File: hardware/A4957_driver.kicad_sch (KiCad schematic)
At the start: 21 parts, among them Q1 PSMN1R0-30YLC,115, Q2 PSMN1R0-30YLC,115, Q3 PSMN1R0-30YLC,115, Q4 PSMN1R0-30YLC,115

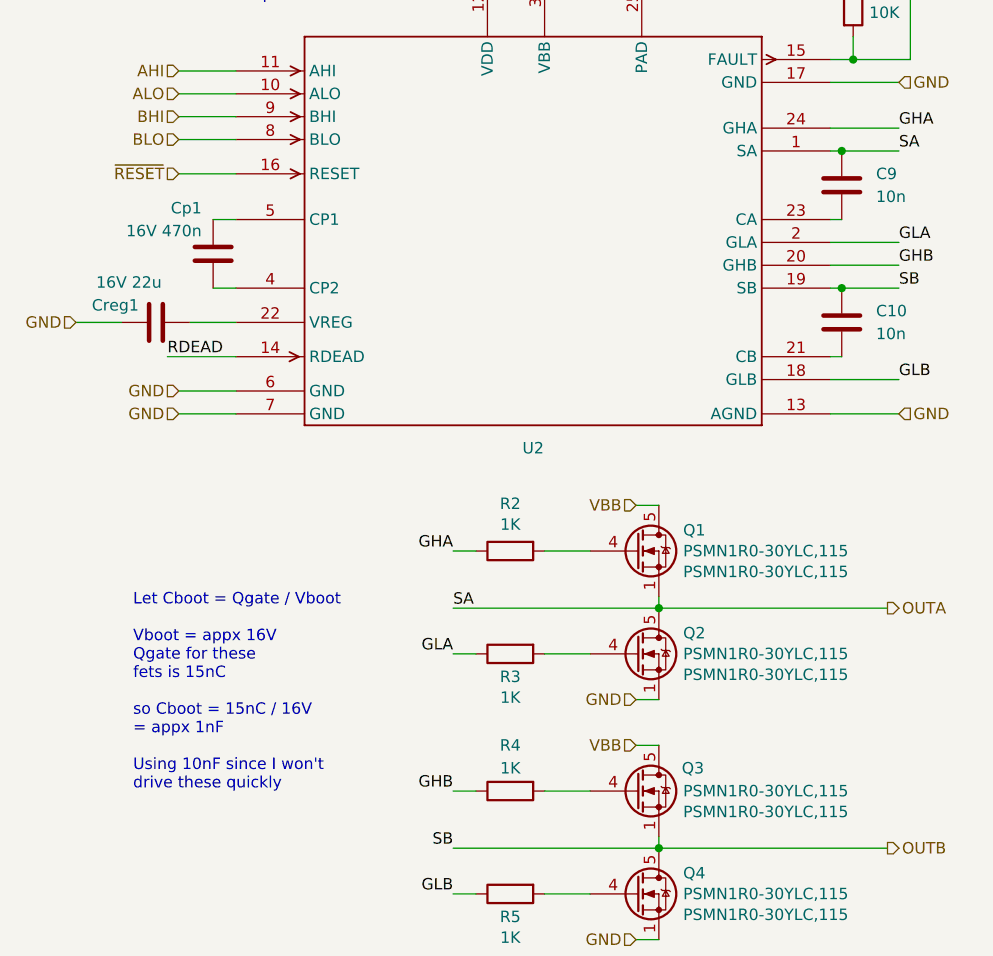
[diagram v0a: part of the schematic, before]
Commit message: initial layout poisitions done
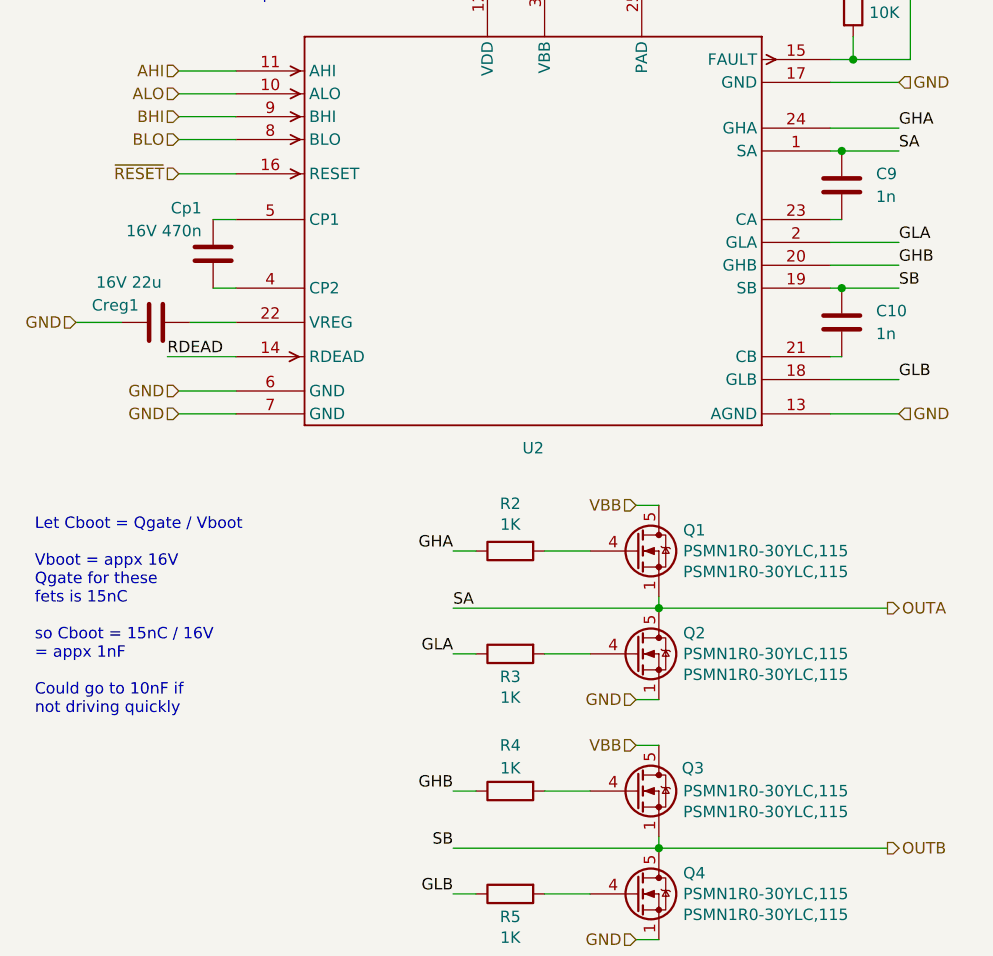
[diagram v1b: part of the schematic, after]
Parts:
- C10, C9: value 10n -> 1n
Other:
- note added: "Let Cboot = Qgate / Vboot Vboot = appx 16V Qgate for these fets is 15nC so Cboot = 15nC / 16V = appx 1nF Could go to 10nF if not driving quickly"
- note removed: "Let Cboot = Qgate / Vboot Vboot = appx 16V Qgate for these fets is 15nC so Cboot = 15nC / 16V = appx 1nF Using 10nF since I won't drive these quickly"
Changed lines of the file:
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@@
 		)
 	)
-	(text "Let Cboot = Qgate / Vboot\n\nVboot = appx 16V\nQgate for these \nfets is 15nC\n\nso Cboot = 15nC / 16V \n= appx 1nF\n\nUsing 10nF since I won't \ndrive these quickly"
-		(exclude_from_sim no)
-		(at 44.45 160.02 0)
+	(text "Let Cboot = Qgate / Vboot\n\nVboot = appx 16V\nQgate for these \nfets is 15nC\n\nso Cboot = 15nC / 16V \n= appx 1nF\n\nCould go to 10nF if\nnot driving quickly"
+		(exclude_from_sim no)
+		(at 33.528 151.638 0)
 		(effects
 			(font
@@
 		(fields_autoplaced yes)
 		(property "Reference" "C10"
-			(at 127 106.68 0)
-			(effects
-				(font
-					(size 1.27 1.27)
-				)
-				(justify left)
-			)
-		)
-		(property "Value" "10n"
-			(at 127 109.22 0)
+			(at 127 106.6799 0)
+			(effects
+				(font
+					(size 1.27 1.27)
+				)
+				(justify left)
+			)
+		)
+		(property "Value" "1n"
+			(at 127 109.2199 0)
 			(effects
 				(font
@@
 		(fields_autoplaced yes)
 		(property "Reference" "C9"
-			(at 127 91.44 0)
-			(effects
-				(font
-					(size 1.27 1.27)
-				)
-				(justify left)
-			)
-		)
-		(property "Value" "10n"
-			(at 127 93.98 0)
-			(effects
-				(font
+			(at 127 91.4399 0)
+			(effects
+				(font
+					(size 1.27 1.27)
+				)
+				(justify left)
+			)
+		)
+		(property "Value" "1n"
+			(at 127 93.9799 0)
+			(effects
+				(font

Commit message: set repo
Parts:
- C10, C9: value 1n -> 1nF; footprint Capacitor_SMD:C_0603_1608Metric -> Capacitor_SMD:C_0805_2012Metric
- C11: value 50V 10U -> 50V 10uF
- C5: value 10U -> 10uF
- C6: value 100N -> 100nF; footprint Capacitor_SMD:C_0603_1608Metric -> Capacitor_SMD:C_0805_2012Metric
- C7, C8: value 50V 220U -> 50V 220uF
- Cp1: value 16V 470n -> 16V 470nF
- Creg1: value 16V 22u -> 16V 22uF
- JP1, R1, R2, R3, R4, R5, R6: footprint Resistor_SMD:R_0603_1608Metric -> Capacitor_SMD:C_0805_2012Metric
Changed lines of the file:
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@@
 			)
 		)
-		(property "Value" "10U"
+		(property "Value" "10uF"
 			(at 79.121 46.863 0)
 			(effects
@@
 			)
 		)
-		(property "Value" "100N"
+		(property "Value" "100nF"
 			(at 88.011 46.863 0)
 			(effects
@@
 			)
 		)
-		(property "Footprint" "Capacitor_SMD:C_0603_1608Metric"
+		(property "Footprint" "Capacitor_SMD:C_0805_2012Metric"
 			(at 84.1248 49.53 0)
 			(effects
@@
 			)
 		)
-		(property "Footprint" "Resistor_SMD:R_0603_1608Metric"
+		(property "Footprint" "Capacitor_SMD:C_0805_2012Metric"
 			(at 86.36 143.002 90)
 			(effects
@@
 			)
 		)
-		(property "Footprint" "Resistor_SMD:R_0603_1608Metric"
+		(property "Footprint" "Capacitor_SMD:C_0805_2012Metric"
 			(at 86.36 131.572 90)
 			(effects
@@
 			)
 		)
-		(property "Footprint" "Resistor_SMD:R_0603_1608Metric"
+		(property "Footprint" "Capacitor_SMD:C_0805_2012Metric"
 			(at 86.36 169.672 90)
 			(effects
@@
 			)
 		)
-		(property "Footprint" "Resistor_SMD:R_0603_1608Metric"
+		(property "Footprint" "Capacitor_SMD:C_0805_2012Metric"
 			(at 86.36 158.242 90)
 			(effects
@@
 			)
 		)
-		(property "Value" "50V 10U"
+		(property "Value" "50V 10uF"
 			(at 128.651 45.593 0)
 			(effects
@@
 			)
 		)
-		(property "Value" "50V 220U"
+		(property "Value" "50V 220uF"
 			(at 104.14 49.53 90)
 			(effects
@@
 			)
 		)
-		(property "Value" "50V 220U"
+		(property "Value" "50V 220uF"
 			(at 113.03 49.53 90)
 			(effects
@@
 			)
 		)
-		(property "Value" "1n"
+		(property "Value" "1nF"
 			(at 127 109.2199 0)
 			(effects
@@
 			)
 		)
-		(property "Footprint" "Capacitor_SMD:C_0603_1608Metric"
+		(property "Footprint" "Capacitor_SMD:C_0805_2012Metric"
 			(at 124.1552 111.76 0)
 			(effects
@@
 			)
 		)
-		(property "Footprint" "Resistor_SMD:R_0603_1608Metric"
+		(property "Footprint" "Capacitor_SMD:C_0805_2012Metric"
 			(at 57.15 59.69 0)
 			(effects
@@
 			)
 		)
-		(property "Footprint" "Resistor_SMD:R_0603_1608Metric"
+		(property "Footprint" "Capacitor_SMD:C_0805_2012Metric"
 			(at 58.42 66.548 90)
 			(effects
@@
 			)
 		)
-		(property "Value" "16V 470n"
+		(property "Value" "16V 470nF"
 			(at 52.07 97.79 0)
 			(effects
@@
 			)
 		)
-		(property "Footprint" "Resistor_SMD:R_0603_1608Metric"
+		(property "Footprint" "Capacitor_SMD:C_0805_2012Metric"
 			(at 122.682 72.39 90)
 			(effects
@@
 			)
 		)
-		(property "Value" "1n"
+		(property "Value" "1nF"
 			(at 127 93.9799 0)
 			(effects
@@
 			)
 		)
-		(property "Footprint" "Capacitor_SMD:C_0603_1608Metric"
+		(property "Footprint" "Capacitor_SMD:C_0805_2012Metric"
 			(at 124.1552 96.52 0)
 			(effects
@@
 			)
 		)
-		(property "Value" "16V 22u"
+		(property "Value" "16V 22uF"
 			(at 47.625 103.505 90)
 			(effects

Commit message: removed old
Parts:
- removed Cp1: 16V 470nF, Capacitor_SMD:C_0805_2012Metric, symbol Device:C
- removed Creg1: 16V 22uF, Capacitor_SMD:C_0805_2012Metric, symbol Device:C
- removed U2: ~, Package_DFN_QFN:HVQFN-24-1EP_4x4mm_P0.5mm_EP2.6x2.6mm_ThermalVias, symbol DMATS_capstone:A4957
- added C13: 16V 470nF, Capacitor_SMD:C_0805_2012Metric_Pad1.18x1.45mm_HandSolder, symbol Device:C
- added C9: 16V 22uF, Capacitor_SMD:C_0805_2012Metric_Pad1.18x1.45mm_HandSolder, symbol Device:C
- added U2: A4957SESTR-T, kml-custom:QFN-24_ALM, symbol kml-custom:A4957SESTR-T
- C10: renamed from C11; footprint Capacitor_SMD:C_0805_2012Metric -> Capacitor_SMD:C_0805_2012Metric_Pad1.18x1.45mm_HandSolder
- C11: renamed from C6; footprint Capacitor_SMD:C_0805_2012Metric -> Capacitor_SMD:C_0805_2012Metric_Pad1.18x1.45mm_HandSolder
- C12: renamed from C5; footprint Capacitor_SMD:C_0805_2012Metric -> Capacitor_SMD:C_0805_2012Metric_Pad1.18x1.45mm_HandSolder
- C7: renamed from C9; footprint Capacitor_SMD:C_0805_2012Metric -> Capacitor_SMD:C_0805_2012Metric_Pad1.18x1.45mm_HandSolder
- C8: renamed from C10; footprint Capacitor_SMD:C_0805_2012Metric -> Capacitor_SMD:C_0805_2012Metric_Pad1.18x1.45mm_HandSolder
- R1: renamed from R2; footprint Capacitor_SMD:C_0805_2012Metric -> Resistor_SMD:R_0805_2012Metric_Pad1.20x1.40mm_HandSolder
- R2: renamed from R3; footprint Capacitor_SMD:C_0805_2012Metric -> Resistor_SMD:R_0805_2012Metric_Pad1.20x1.40mm_HandSolder
- R3: renamed from R4; footprint Capacitor_SMD:C_0805_2012Metric -> Resistor_SMD:R_0805_2012Metric_Pad1.20x1.40mm_HandSolder
- R4: renamed from R5; footprint Capacitor_SMD:C_0805_2012Metric -> Resistor_SMD:R_0805_2012Metric_Pad1.20x1.40mm_HandSolder
- R5: renamed from R6; footprint Capacitor_SMD:C_0805_2012Metric -> Resistor_SMD:R_0805_2012Metric_Pad1.20x1.40mm_HandSolder
- Rdead1: renamed from R1; value 10K -> 3k; footprint Capacitor_SMD:C_0805_2012Metric -> Resistor_SMD:R_0805_2012Metric_Pad1.20x1.40mm_HandSolder
- renumbered C7 to C5, C8 to C6
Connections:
- net ALO: now also U2.10 (ALO)
- net BHI: now also U2.9 (BHI)
- net BLO: now also U2.8 (BLO)
- net GHA: now also U2.24 (GHA)
- net GHB: now also U2.20 (GHB)
- net GLA: now also U2.2 (GLA)
- net GLB: now also U2.18 (GLB)
- net GND: now also C9.2, U2.17 (GND), U2.25 (PAD), U2.6 (GND), U2.7 (GND)
- net OUTA: now also U2.1 (SA)
- net OUTB: now also U2.19 (SB)
- net RDEAD: now also U2.14 (RDEAD)
- net VBB: now also U2.3 (VBB)
- net VDD: now also U2.12 (VDD)
- net ~{FAULT}: now also U2.15 (FAULT)
- net ~{RESET}: now also U2.16 (RESET)
- net CB: now reaches C8.2
- net CB: now also U2.21 (CB)
- net CA: now reaches C7.2
- net CA: now also U2.23 (CA)
- new net: C13.2, U2.4 (CP2)
- new net: C13.1, U2.5 (CP1)
- new net ALI: U2.11 (ALI)
- new net GNDA: U2.13 (AGND)
- new net VREG: C9.1, U2.22 (VREG)
- no-connect marks 1 -> 0
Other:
- note added: "Bootstrap Caps"
- note added: "Dead-time Configuration"
- note added: "H-Bridge Gate Driver"
- note added: "Let Cboot = Qgate / Vboot Vboot = appx 16V Qgate for these fets is 15nC Cboot = 15nC / 16V =~ 1nF Could go to 10nF if not driving quick enough"
- note added: "MOSFET H-Bridge N-CH 30V 100A"
- note added: "RDEAD -> Rdead -> GND: t_DEAD ≈ 50 + 7200 / (1.2 + (200 / R_DEAD)) -> for R_DEAD > 3kOhms -> see datasheet for curve RDEAD -> VDD: 6µs dead time RDEAD -> GND: no dead time, must be supplied by controller -> i.e. logic control signals must incorporate dead time"
- note removed: "Let Cboot = Qgate / Vboot Vboot = appx 16V Qgate for these fets is 15nC so Cboot = 15nC / 16V = appx 1nF Could go to 10nF if not driving quickly"
- note removed: "RDEAD -> VDD = 6µs dead time"
- moved on the sheet: C10, C11, C12, C5, C6, C7, C8, JP1, Q1, Q2, Q3, Q4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
